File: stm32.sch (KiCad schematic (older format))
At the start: 33 parts, among them P1 USB_OTG, P2 CONN_01X04, U3 STM32F407VETx, U4 USBLC6-4SC6, Y2 25M, Y3 RTC

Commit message: finish routing of bottom board
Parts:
- removed C55: 1n, stmbl:C_0603, symbol stmbl:C
- added C77, C78: 18p, stmbl:C_0603, symbol stmbl:C
- added J10: CONN_01X02, stmbl:Pin_Header_Straight_1x02, symbol stmbl:CONN_01X02
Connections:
- net GND: now also C44.2, C45.2, C77.2, C78.2; no longer Y3.1
- net STM_CS: now also U3.53 (PB14); no longer U3.93 (PB7)
- net SWCLK: now also U4.4 (IO3); no longer U4.6 (IO4)
- net SWIO: now also U4.6 (IO4); no longer U4.4 (IO3)
- net at U3.54 (PB15): no longer Y3.2
- net USART3_TX: now reaches U3.55 (PD8)
- net USART3_TX: now also J10.2 (Pin_2)
- net USART3_RX: now reaches U3.56 (PD9)
- net USART3_RX: now also J10.1 (Pin_1)
- net at U3.8 (PC14): now also Y3.1, C77.1
- net at U3.9 (PC15): now also Y3.2, C78.1
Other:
- moved on the sheet: Y3
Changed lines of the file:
@@
 Wire Wire Line
 	14900 5950 15000 5950
-Text HLabel 8850 5700 0    60   Input ~ 0
+Text HLabel 8850 6400 0    60   Input ~ 0
 STM_CS
 $Comp
@@
 	8850 3300 8950 3300
 Wire Wire Line
-	8950 5700 8850 5700
+	8950 6400 8850 6400
 Wire Wire Line
 	11250 3700 11400 3700
@@
 Wire Wire Line
 	11250 3600 11400 3600
-Text GLabel 14200 4450 1    60   Input ~ 0
-DC_LINK
-$Comp
-L stmbl:C C55
-U 1 1 5E66E91A
-P 14200 4700
-F 0 "C55" H 14085 4654 50  0000 R CNN
-F 1 "1n" H 14085 4745 50  0000 R CNN
-F 2 "stmbl:C_0603" H 14238 4550 50  0001 C CNN
-F 3 "" H 14200 4700 50  0000 C CNN
-F 4 "" H 0   0   50  0001 C CNN "Manufacturer No"
-F 5 "" H 0   0   50  0001 C CNN "Source"
-F 6 "X5R" H 0   0   50  0001 C CNN "Tolerance"
-F 7 "50V" H 0   0   50  0001 C CNN "Voltage"
-	1    14200 4700
-	-1   0    0    1
-$EndComp
-$Comp
-L stmbl:GND #PWR0152
-U 1 1 5E66E972
-P 14200 4950
-F 0 "#PWR0152" H 14200 4700 50  0001 C CNN
-F 1 "GND" V 14205 4822 50  0000 R CNN
-F 2 "" H 14200 4950 50  0000 C CNN
-F 3 "" H 14200 4950 50  0000 C CNN
-	1    14200 4950
-	1    0    0    -1
-$EndComp
-Wire Wire Line
-	14200 4950 14200 4850
-Wire Wire Line
-	14200 4550 14200 4450
 Wire Wire Line
 	11250 4500 11350 4500
 Wire Wire Line
 	8850 4000 8950 4000
+Text GLabel 14850 1850 2    60   Input ~ 0
+SWIO
 Text GLabel 14850 2250 2    60   Input ~ 0
-SWIO
-Text GLabel 14850 1850 2    60   Input ~ 0
 SWCLK
 $Comp
@@
 	7850 3400 8000 3400
 Wire Wire Line
-	8300 1800 8300 2400
+	8300 1800 8300 2100
 Wire Wire Line
 	12850 1250 13100 1250
@@
 L stmbl:Crystal Y3
 U 1 1 5D421BBB
-P 8950 6750
-F 0 "Y3" V 8996 6619 50  0000 R CNN
-F 1 "RTC" V 8905 6619 50  0000 R CNN
-F 2 "stmbl:Crystal_SMD_0603_4Pads" H 8950 6750 50  0001 C CNN
-F 3 "" H 8950 6750 50  0000 C CNN
-F 4 "LFXTAL061642Reel" H 300 4650 50  0001 C CNN "Manufacturer No"
-F 5 "Mouser 449-LFXTAL061642REEL" H 300 4650 50  0001 C CNN "Source"
-F 6 "" H 300 4650 50  0001 C CNN "Tolerance"
-F 7 "" H 300 4650 50  0001 C CNN "Voltage"
-	1    8950 6750
-	0    -1   -1   0
-$EndComp
-Wire Wire Line
-	8950 6500 8950 6600
-$Comp
-L stmbl:GND #PWR0161
-U 1 1 5D42CB08
-P 8950 7000
-F 0 "#PWR0161" H 8950 6750 50  0001 C CNN
-F 1 "GND" H 8955 6827 50  0000 C CNN
-F 2 "" H 8950 7000 50  0000 C CNN
-F 3 "" H 8950 7000 50  0000 C CNN
-	1    8950 7000
-	1    0    0    -1
-$EndComp
-Wire Wire Line
-	8950 7000 8950 6900
+P 11550 6450
+F 0 "Y3" V 11596 6319 50  0000 R CNN
+F 1 "RTC" V 11505 6319 50  0000 R CNN
+F 2 "stmbl:Crystal_SMD_0603_4Pads" H 11550 6450 50  0001 C CNN
+F 3 "" H 11550 6450 50  0000 C CNN
+F 4 "LFXTAL061642Reel" H 2900 4350 50  0001 C CNN "Manufacturer No"
+F 5 "Mouser 449-LFXTAL061642REEL" H 2900 4350 50  0001 C CNN "Source"
+F 6 "" H 2900 4350 50  0001 C CNN "Tolerance"
+F 7 "" H 2900 4350 50  0001 C CNN "Voltage"
+	1    11550 6450
+	0    1    1    0
+$EndComp
 Wire Wire Line
 	10500 800  10400 800
@@
 Wire Wire Line
 	15400 8850 15400 8950
+Connection ~ 8300 2100
+Wire Wire Line
+	8300 2100 8300 2400
+Wire Wire Line
+	11250 6400 11350 6400
+Wire Wire Line
+	11350 6400 11350 6300
+Wire Wire Line
+	11250 6500 11350 6500
+Wire Wire Line
+	11350 6500 11350 6600
+$Comp
+L stmbl:C C78
+U 1 1 5E2C6F77
+P 11850 6600
+F 0 "C78" V 11700 6600 50  0000 C CNN
+F 1 "18p" V 12000 6600 50  0000 C CNN
+F 2 "stmbl:C_0603" H 11888 6450 50  0001 C CNN
+F 3 "" H 11850 6600 50  0000 C CNN
+F 4 "" H 3400 4200 50  0001 C CNN "Manufacturer No"
+F 5 "" H 3400 4200 50  0001 C CNN "Source"
+F 6 "X5R" H 3400 4200 50  0001 C CNN "Tolerance"
+F 7 "50V" H 3400 4200 50  0001 C CNN "Voltage"
+	1    11850 6600
+	0    -1   -1   0
+$EndComp
+$Comp
+L stmbl:C C77
+U 1 1 5E2C7D41
+P 11850 6300
+F 0 "C77" V 11700 6300 50  0000 C CNN
+F 1 "18p" V 12000 6300 50  0000 C CNN
+F 2 "stmbl:C_0603" H 11888 6150 50  0001 C CNN
+F 3 "" H 11850 6300 50  0000 C CNN
+F 4 "" H 3400 3900 50  0001 C CNN "Manufacturer No"
+F 5 "" H 3400 3900 50  0001 C CNN "Source"
+F 6 "X5R" H 3400 3900 50  0001 C CNN "Tolerance"
+F 7 "50V" H 3400 3900 50  0001 C CNN "Voltage"
+	1    11850 6300
+	0    -1   -1   0
+$EndComp
+Wire Wire Line
+	12000 6300 12100 6300
+Wire Wire Line
+	12100 6300 12100 6600
+Wire Wire Line
+	12100 6600 12000 6600
+$Comp
+L stmbl:GND #PWR0161
+U 1 1 5E2D8C15
+P 12100 6650
+F 0 "#PWR0161" H 12100 6400 50  0001 C CNN
+F 1 "GND" V 12105 6522 50  0000 R CNN
+F 2 "" H 12100 6650 50  0000 C CNN
+F 3 "" H 12100 6650 50  0000 C CNN
+	1    12100 6650
+	1    0    0    -1
+$EndComp
+Wire Wire Line
+	12100 6650 12100 6600
+Connection ~ 12100 6600
+Wire Wire Line
+	11350 6300 11550 6300
+Wire Wire Line
+	11350 6600 11550 6600
+Connection ~ 11550 6300
+Wire Wire Line
+	11550 6300 11700 6300
+Connection ~ 11550 6600
+Wire Wire Line
+	11550 6600 11700 6600
+Text GLabel 11400 4000 2    50   Input ~ 0
+USART3_TX
+Text GLabel 11400 4100 2    50   Input ~ 0
+USART3_RX
+Wire Wire Line
+	11250 4000 11400 4000
+Wire Wire Line
+	11250 4100 11400 4100
+Text GLabel 13500 4100 0    50   Input ~ 0
+USART3_TX
+Text GLabel 13500 4000 0    50   Input ~ 0
+USART3_RX
+$Comp
+L stmbl:CONN_01X02 J10
+U 1 1 5E5A4DE9
+P 13900 4000
+F 0 "J10" H 13980 3992 50  0000 L CNN
+F 1 "CONN_01X02" H 13980 3901 50  0000 L CNN
+F 2 "stmbl:Pin_Header_Straight_1x02" H 13900 4000 50  0001 C CNN
+F 3 "" H 13900 4000 50  0001 C CNN
+	1    13900 4000
+	1    0    0    -1
+$EndComp
+Wire Wire Line
+	13500 4000 13700 4000
+Wire Wire Line
+	13500 4100 13700 4100
 $EndSCHEMATC

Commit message: V2 hardware
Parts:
- removed J10: CONN_01X02, stmbl:Pin_Header_Straight_1x02, symbol stmbl:CONN_01X02
- added J16: Conn_02x20_Odd_Even, Connector_PinHeader_2.54mm:PinHeader_2x20_P2.54mm_Vertical, symbol Connector_Generic:Conn_02x20_Odd_Even
- Y2: footprint stmbl:Crystal_SMD_0603_4Pads -> Crystal:Crystal_SMD_3225-4Pin_3.2x2.5mm; symbol stmbl:Crystal -> Device:Crystal_GND24
- Y3: footprint stmbl:Crystal_SMD_0603_4Pads -> Crystal:Crystal_SMD_3215-2Pin_3.2x1.5mm; symbol stmbl:Crystal -> Device:Crystal
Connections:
- net +3V3: now also J16.1 (Pin_1), J16.17 (Pin_17)
- net GND: now also J16.14 (Pin_14), J16.20 (Pin_20), J16.25 (Pin_25), J16.30 (Pin_30), J16.34 (Pin_34), J16.39 (Pin_39), J16.6 (Pin_6), J16.9 (Pin_9)
- net STM_SPI1MISO: now also U3.31 (PA6); no longer U3.90 (PB4)
- net STM_SPI1SCK: now also U3.30 (PA5); no longer U3.89 (PB3)
- net SWCLK: now also U4.6 (IO4); no longer U4.4 (IO3)
- net SWIO: now also U4.4 (IO3); no longer U4.6 (IO4)
- net USART3_RX: now also U3.79 (PC11), J16.10 (Pin_10); no longer U3.56 (PD9)
- net USART3_TX: now also U3.78 (PC10), J16.8 (Pin_8); no longer U3.55 (PD8)
- net at U3.1 (PE2): now also D28.2 (A)
- net at C44.1, U3.12 (PH0/OSC_IN/EVENTOUT): now also Y2.3; no longer Y2.2
- net at U3.2 (PE3): now also D29.2 (A)
- net at U3.3 (PE4): now also D30.2 (A)
- net MMDVM_NRST: now reaches U3.77 (PA15)
- net MMDVM_NRST: now also J16.40 (Pin_40)
- net MMDVM_BOOT0: now reaches U3.80 (PC12)
- net MMDVM_BOOT0: now also J16.38 (Pin_38)
- net at U3.85 (PD4): no longer D28.2 (A)
- net at U3.86 (PD5): no longer D29.2 (A)
- net at U3.87 (PD6): no longer D30.2 (A)
- net MMDVM_GPIO5: now reaches U3.92 (PB6)
- net MMDVM_GPIO4: now reaches U3.93 (PB7)
- net MMDVM_GPIO4: now also J16.7 (Pin_7)
- net MMDVM_GPIO3: now reaches U3.95 (PB8)
- net MMDVM_GPIO3: now also J16.5 (Pin_5)
- net MMDVM_GPIO2: now reaches U3.96 (PB9)
- net MMDVM_GPIO2: now also J16.4 (Pin_4)
- net MMDVM_GPIO1: now reaches U3.97 (PE0)
- net MMDVM_GPIO1: now also J16.3 (Pin_3)
- net MMDVM_GPIO0: now reaches U3.98 (PE1)
- net MMDVM_GPIO0: now also J16.2 (Pin_2)
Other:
- moved on the sheet: D28, D29, D30, R64, R65, R66

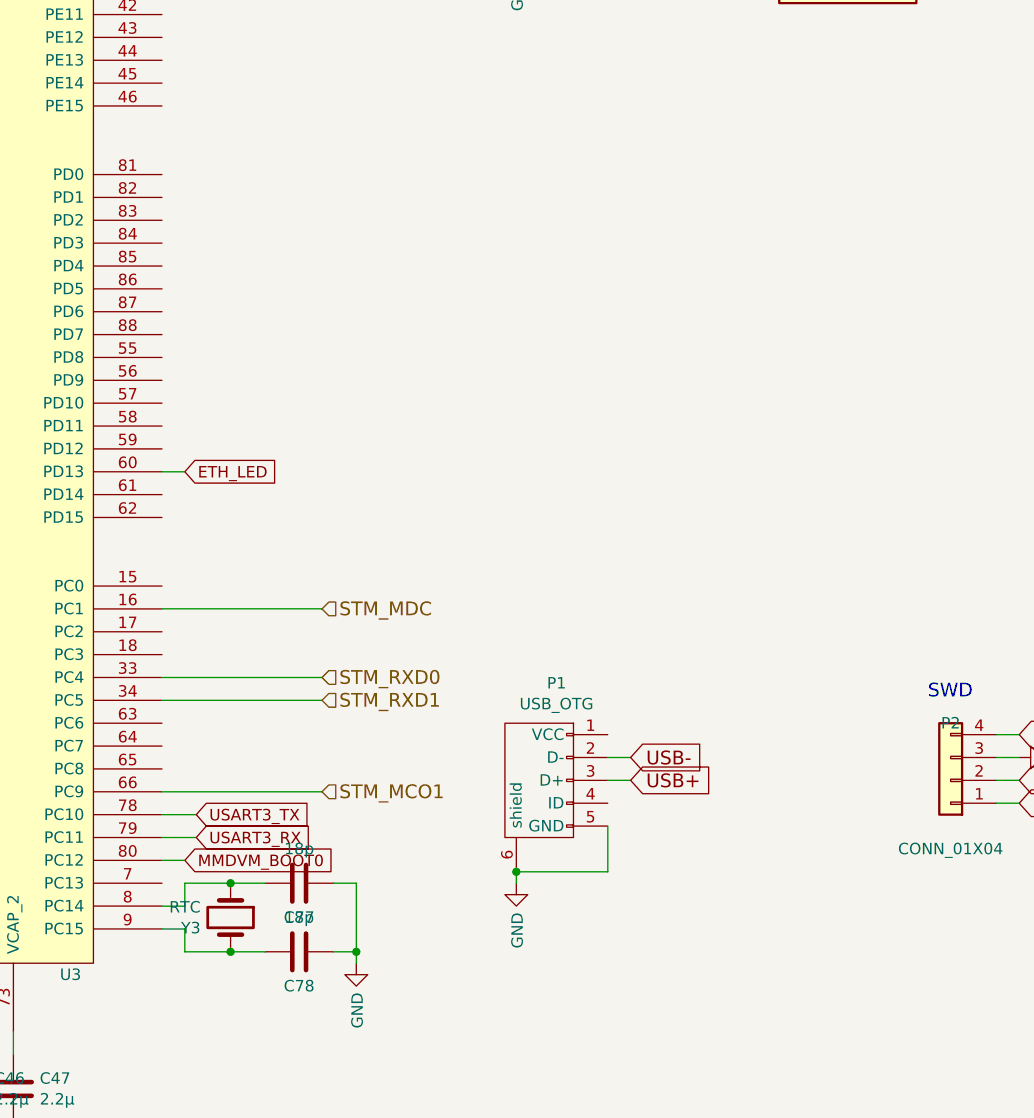
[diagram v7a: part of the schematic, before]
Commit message: add sd card holder
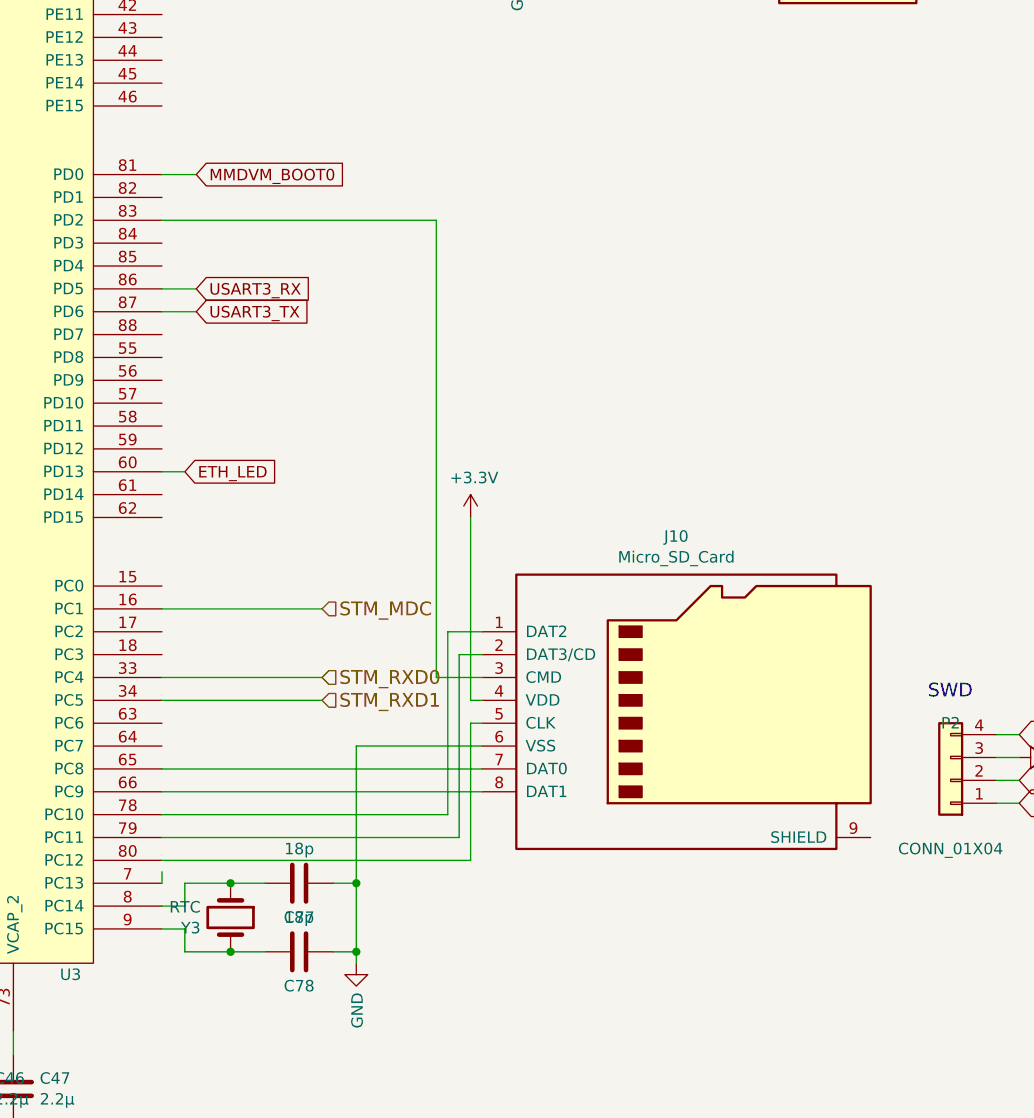
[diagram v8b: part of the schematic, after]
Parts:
- removed P1: USB_OTG, stmbl:USB_Micro-B, symbol stmbl:USB_OTG
- added J10: Micro_SD_Card, Connector_Card:microSD_HC_Hirose_DM3D-SF, symbol Connector:Micro_SD_Card
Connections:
- net +3V3: now also J10.4 (VDD)
- net GND: now also J10.6 (VSS)
- net MMDVM_BOOT0: now also U3.81 (PD0); no longer U3.80 (PC12)
- net USART3_RX: now also U3.86 (PD5); no longer U3.79 (PC11)
- net USART3_TX: now also U3.87 (PD6); no longer U3.78 (PC10)
- net at U3.65 (PC8): now also J10.7 (DAT0)
- net at U3.83 (PD2): now also J10.3 (CMD)
- net STM_MCO1: no longer names the net of U3.66 (PC9)
- net STM_MCO1: now also J10.8 (DAT1)
- new net: J10.1 (DAT2), U3.78 (PC10)
- new net: J10.2 (DAT3/CD), U3.79 (PC11)
- new net: J10.5 (CLK), U3.80 (PC12)
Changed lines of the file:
@@
 Text HLabel 11950 5100 2    60   Input ~ 0
 STM_MDC
-Text GLabel 13300 5850 2    60   Input ~ 0
-USB+
-Text GLabel 13300 5750 2    60   Input ~ 0
-USB-
 Text GLabel 8850 4400 0    60   Input ~ 0
 USB+
@@
 Text GLabel 8850 4500 0    60   Input ~ 0
 SWIO
-Text HLabel 11950 5900 2    60   Input ~ 0
-STM_MCO1
 Text HLabel 8850 3900 0    60   Input ~ 0
 STM_CRS
-$Comp
-L stmbl:GND #PWR0138
-U 1 1 57FF4076
-P 12800 6300
-F 0 "#PWR0138" H 12800 6050 50  0001 C CNN
-F 1 "GND" V 12805 6172 50  0000 R CNN
-F 2 "" H 12800 6300 50  0000 C CNN
-F 3 "" H 12800 6300 50  0000 C CNN
-	1    12800 6300
-	1    0    0    -1
-$EndComp
 Text HLabel 8300 5500 0    60   Input ~ 0
 STM_SPI1MOSI
@@
 	11250 5100 11950 5100
 Wire Wire Line
-	13200 5750 13300 5750
-Wire Wire Line
-	13200 5850 13300 5850
-Wire Wire Line
 	8400 1600 8700 1600
 Connection ~ 8700 1600
 Wire Wire Line
-	11250 5900 11950 5900
-Wire Wire Line
 	8950 4500 8850 4500
 Wire Wire Line
@@
 Wire Wire Line
 	8950 4400 8850 4400
-Wire Wire Line
-	12800 6250 12800 6300
 Text GLabel 8850 4300 0    60   Input ~ 0
 USB-
@@
 	8600 2400 8650 2400
 Wire Wire Line
-	13200 6050 13200 6250
-Wire Wire Line
-	13200 6250 12800 6250
-Wire Wire Line
 	8950 5500 8300 5500
 Wire Wire Line
@@
 Text GLabel 11350 4500 2    50   Input ~ 0
 ETH_LED
-$Comp
-L stmbl:USB_OTG P1
-U 1 1 5B9CAF4B
-P 12900 5850
-F 0 "P1" V 12475 5774 50  0000 C CNN
-F 1 "USB_OTG" V 12566 5774 50  0000 C CNN
-F 2 "stmbl:USB_Micro-B" V 12850 5750 50  0001 C CNN
-F 3 "" V 12850 5750 50  0000 C CNN
-F 4 "ZX62D-B-5PA8(30)" H 0   0   50  0001 C CNN "Manufacturer No"
-F 5 "Mouser 798-ZX62D-B-5PA830" H 0   0   50  0001 C CNN "Source"
-F 6 "" H 0   0   50  0001 C CNN "Tolerance"
-F 7 "" H 0   0   50  0001 C CNN "Voltage"
-	1    12900 5850
-	0    -1   1    0
-$EndComp
 Wire Wire Line
 	8700 1500 8700 1600
@@
 Wire Wire Line
 	12850 950  13100 950
-Connection ~ 12800 6250
 Wire Wire Line
 	10500 800  10400 800
@@
 	12100 6650 12100 6600
 Connection ~ 12100 6600
-Text GLabel 11400 6000 2    50   Input ~ 0
+Text GLabel 11400 3800 2    50   Input ~ 0
 USART3_TX
-Text GLabel 11400 6100 2    50   Input ~ 0
+Text GLabel 11400 3700 2    50   Input ~ 0
 USART3_RX
 Wire Wire Line
-	11250 6000 11400 6000
-Wire Wire Line
-	11250 6100 11400 6100
+	11250 3700 11400 3700
+Wire Wire Line
+	11250 3800 11400 3800
 Wire Wire Line
 	11550 6600 11700 6600
@@
 Wire Wire Line
 	4550 3850 4050 3850
-Text GLabel 11350 6200 2    50   Input ~ 0
+Text GLabel 11400 3200 2    50   Input ~ 0
 MMDVM_BOOT0
 Text GLabel 8850 4700 0    50   Input ~ 0
@@
 Wire Wire Line
 	8850 4700 8950 4700
-Wire Wire Line
-	11350 6200 11250 6200
 Text GLabel 4550 5250 2    50   Input ~ 0
 MMDVM_BOOT0
@@
 Wire Wire Line
 	2950 3750 3550 3750
+$Comp
+L Connector:Micro_SD_Card J10
+U 1 1 5D1E742C
+P 13550 5500
+F 0 "J10" H 13500 6217 50  0000 C CNN
+F 1 "Micro_SD_Card" H 13500 6126 50  0000 C CNN
+F 2 "Connector_Card:microSD_HC_Hirose_DM3D-SF" H 14700 5800 50  0001 C CNN
+F 3 "http://katalog.we-online.de/em/datasheet/693072010801.pdf" H 13550 5500 50  0001 C CNN
+	1    13550 5500
+	1    0    0    -1
+$EndComp
+Wire Wire Line
+	11250 5900 12650 5900
+Wire Wire Line
+	11250 5800 12650 5800
+Wire Wire Line
+	12100 6300 12100 5700
+Wire Wire Line
+	12100 5700 12650 5700
+Connection ~ 12100 6300
+Wire Wire Line
+	12650 5300 12550 5300
+Wire Wire Line
+	12550 5300 12550 6100
+Wire Wire Line
+	12550 6100 11250 6100
+Wire Wire Line
+	11250 6000 12500 6000
+Wire Wire Line
+	12500 6000 12500 5200
+Wire Wire Line
+	12500 5200 12650 5200
+Wire Wire Line
+	11250 6300 11250 6250
+Wire Wire Line
+	11250 3200 11400 3200
+Wire Wire Line
+	11250 6200 12600 6200
+Wire Wire Line
+	12600 6200 12600 5600
+Wire Wire Line
+	12600 5600 12650 5600
+Wire Wire Line
+	11250 3400 12450 3400
+Wire Wire Line
+	12450 3400 12450 5400
+Wire Wire Line
+	12450 5400 12650 5400
+Wire Wire Line
+	12650 5500 12600 5500
+Wire Wire Line
+	12600 5500 12600 4700
+$Comp
+L stmbl:+3.3V #PWR?
+U 1 1 5D1EBB18
+P 12600 4700
+AR Path="/5D1EBB18" Ref="#PWR?"  Part="1"
+AR Path="/57A8F795/5D1EBB18" Ref="#PWR?"  Part="1"
+AR Path="/5B42E6A4/5D1EBB18" Ref="#PWR?"  Part="1"
+AR Path="/5D9E315F/5D1EBB18" Ref="#PWR0138"  Part="1"
+F 0 "#PWR0138" H 12600 4550 50  0001 C CNN
+F 1 "+3.3V" H 12615 4873 50  0000 C CNN
+F 2 "" H 12600 4700 50  0000 C CNN
+F 3 "" H 12600 4700 50  0000 C CNN
+	1    12600 4700
+	1    0    0    -1
+$EndComp
 $EndSCHEMATC
